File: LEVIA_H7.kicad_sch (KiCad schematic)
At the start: 4 parts, among them U3 USBLC6-2P6

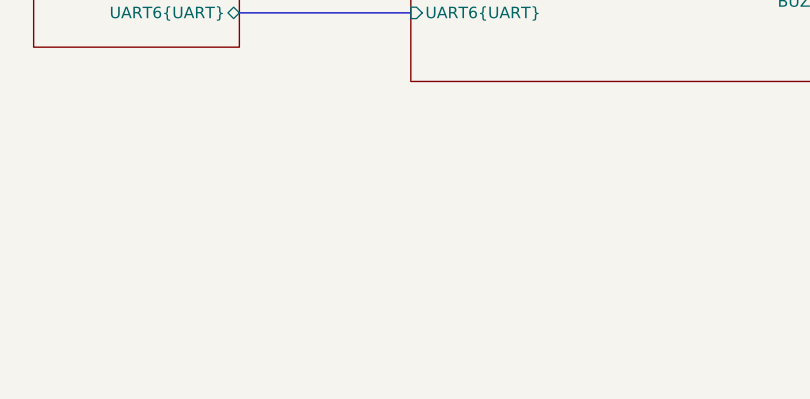
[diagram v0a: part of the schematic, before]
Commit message: imported symbols in PCB, fixed underscore in names
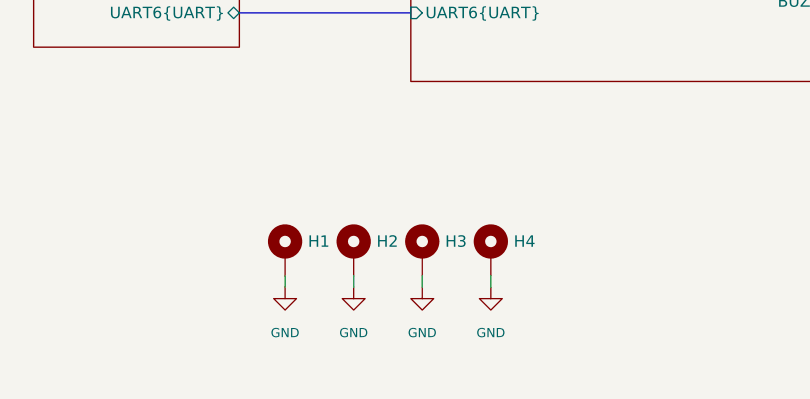
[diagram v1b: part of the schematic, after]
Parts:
- added H1, H2, H3, H4: MountingHole_Pad, MountingHole:MountingHole_3.2mm_M3_DIN965_Pad_TopBottom, symbol Mechanical:MountingHole_Pad
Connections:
- net GND: now also H1.1, H2.1, H3.1, H4.1
